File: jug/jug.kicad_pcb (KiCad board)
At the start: 2 copper layers, 154.4 x 108.2 mm, 96 parts, among them J1 USB_A, J2 USB_A, U1 RP2040_Pro_Micro, U2 RP2040_Pro_Micro

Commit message: finished pcb with RP2040 Pro Micro
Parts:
- removed D28, D29, D30, D31, D32, D33, D34, D35, D36, D37, D38, D39, D40, D41, D42, D43, D44, D45, D46, D47: D, ScottoKeebs_Components:Double_Sided_Diode_DO-35
- removed J2: USB_A, Connector_USB:USB_A_Molex_67643_Horizontal
- removed S24, S25, S26, S27, S28, S29, S30, S31, S32, S33, S34, S35, S36, S37, S38, S39, S40, S41, S42, S43, S44: Keyswitch, ScottoKeebs_Hotswap:Hotswap_MX_Plated_1.00u
- removed S45, S46: Keyswitch, ScottoKeebs_Hotswap:Hotswap_MX_Plated_1.50u_90deg
- removed U1: RP2040_Pro_Micro, ScottoKeebs_MCU:RP2040_Pro_Micro
- added D26: LED, LED_SMD:LED_1206_3216Metric_Pad1.42x1.75mm_HandSolder, F.Cu at (181.7, 114.8)
- added G***: LOGO, LOGO, F.Cu at (190.1, 74.7)
- added G***: LOGO, LOGO, B.Cu at (190.1, 74.7)
- added JP1: SolderJumper_2_Open, Jumper:SolderJumper-2_P1.3mm_Open_TrianglePad1.0x1.5mm, F.Cu at (181.0, 105.1)
- added JP2: SolderJumper_2_Open, Jumper:SolderJumper-2_P1.3mm_Open_TrianglePad1.0x1.5mm, F.Cu at (184.8, 105.1)
- added JP3: SolderJumper_2_Open, Jumper:SolderJumper-2_P1.3mm_Open_TrianglePad1.0x1.5mm, B.Cu at (181.0, 105.1)
- added JP4: SolderJumper_2_Open, Jumper:SolderJumper-2_P1.3mm_Open_TrianglePad1.0x1.5mm, B.Cu at (184.8, 105.1)
- added JP5: SolderJumper_2_Open, Jumper:SolderJumper-2_P1.3mm_Open_TrianglePad1.0x1.5mm, F.Cu at (181.0, 108.5)
- added JP6: SolderJumper_2_Open, Jumper:SolderJumper-2_P1.3mm_Open_TrianglePad1.0x1.5mm, F.Cu at (184.8, 108.5)
- added JP7: SolderJumper_2_Open, Jumper:SolderJumper-2_P1.3mm_Open_TrianglePad1.0x1.5mm, B.Cu at (181.0, 108.5)
- added JP8: SolderJumper_2_Open, Jumper:SolderJumper-2_P1.3mm_Open_TrianglePad1.0x1.5mm, B.Cu at (184.8, 108.5)
- added R1: R, Resistor_SMD:R_1206_3216Metric_Pad1.30x1.75mm_HandSolder, B.Cu at (186.4, 123.2)
- added R2: R, Resistor_SMD:R_1206_3216Metric_Pad1.30x1.75mm_HandSolder, B.Cu at (188.9, 120.7)
- added R3: R, Resistor_SMD:R_1206_3216Metric_Pad1.30x1.75mm_HandSolder, F.Cu at (186.4, 123.2)
- added R4: R, Resistor_SMD:R_1206_3216Metric_Pad1.30x1.75mm_HandSolder, F.Cu at (188.9, 120.7)
- D24, D25: value D -> LED; footprint ScottoKeebs_Components:Double_Sided_Diode_DO-35 -> LED_SMD:LED_1206_3216Metric_Pad1.42x1.75mm_HandSolder; moved to B.Cu
- D27: value D -> LED; footprint ScottoKeebs_Components:Double_Sided_Diode_DO-35 -> LED_SMD:LED_1206_3216Metric_Pad1.42x1.75mm_HandSolder
- S10, S11, S12, S13, S14, S15, S16, S17, S18, S19, S2, S20, S21, S3, S4, S5, S6, S7, S8, S9: footprint ScottoKeebs_Hotswap:Hotswap_MX_Plated_1.00u -> ScottoKeebs_Hotswap:Hotswap_MX_Plated_1.00u_Reversible
- S22, S23: footprint ScottoKeebs_Hotswap:Hotswap_MX_Plated_1.50u_90deg -> ScottoKeebs_Hotswap:Hotswap_MX_Plated_1.50u_90deg_Reversible
- U2: value RP2040_Pro_Micro -> Arduino_Pro_Micro; footprint ScottoKeebs_MCU:RP2040_Pro_Micro -> keyboard_reversible:ProMicro_flipped
- moved U2 318.6 mm to (190.2, 85.7), turned to -90 degrees
- moved D25 310.3 mm to (185.5, 114.8), turned to 90 degrees
- moved D27 309.1 mm to (185.5, 114.8), turned to 90 degrees
- moved D24 292.0 mm to (181.7, 114.8), turned to 90 degrees
- moved J1 45.2 mm to (189.8, 113.8)
- moved S22 42.8 mm to (183.8, 135.7), turned to -26.5 degrees
- moved S14 42.8 mm to (92.7, 115.7), turned to 0 degrees
- moved S4 42.8 mm to (130.8, 65.7), turned to 0 degrees
- moved D2 42.8 mm to (102.2, 81.4)
- moved S16 42.8 mm to (130.8, 103.8), turned to 0 degrees
- moved S8 42.8 mm to (92.7, 96.6), turned to 0 degrees
- moved D1 42.8 mm to (83.2, 83.8)
- moved D6 42.8 mm to (178.4, 81.4)
- moved D12 42.8 mm to (178.4, 100.4)
- moved S5 42.8 mm to (149.9, 72.8), turned to 0 degrees
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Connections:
- D24 pad 1: ROW0R -> Net-(D24-K)
- D24 pad 2: Net-(D24-A) -> LED0
- D25 pad 1: ROW1R -> Net-(D25-K)
- D25 pad 2: Net-(D25-A) -> LED1
- D27 pad 1: ROW2R -> Net-(D27-K)
- D27 pad 2: Net-(D27-A) -> LED1
- J1 pad 1: +5V -> Net-(J1-VBUS)
- J1 pad 2: INTERCONNECT_A -> Net-(J1-D-)
- J1 pad 3: INTERCONNECT_B -> Net-(J1-D+)
- J1 pad 4: GND -> Net-(J1-GND)
- U2 pad 10: COL2R -> unconnected-(U2-7/PE6-Pad10)_1
- U2 pad 11: COL3R -> LED0
- U2 pad 12: COL4R -> LED1
- U2 pad 13: COL5R -> COL5L
- U2 pad 14: unconnected-(U2-GP12-Pad14) -> COL4L
- U2 pad 15: unconnected-(U2-GP13-Pad15) -> COL3L
- U2 pad 16: unconnected-(U2-GP14-Pad16) -> COL2L
- U2 pad 17: unconnected-(U2-GP15-Pad17) -> COL1L
- U2 pad 18: unconnected-(U2-GP16-Pad18) -> COL0L
- U2 pad 19: unconnected-(U2-GP21-Pad19) -> INTERCONNECT_B
- U2 pad 20: unconnected-(U2-GP23-Pad20) -> INTERCONNECT_A
- U2 pad 22: ROW3R -> unconnected-(U2-RST-Pad22)_1
- U2 pad 23: ROW2R -> GND
- U2 pad 24: ROW1R -> +5V
- U2 pad 3: unconnected-(U2-GP1-Pad3) -> GND
- U2 pad 5: GND -> unconnected-(U2-2/PD1-Pad5)_1
- U2 pad 6: INTERCONNECT_A2 -> ROW0L
- U2 pad 7: INTERCONNECT_B2 -> ROW1L
- U2 pad 8: COL0R -> ROW2L
- U2 pad 9: COL1R -> ROW3L
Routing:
- net COL4L: track 185.7 -> 128.6 mm
- net GND: track 0.00 -> 49.2 mm, vias 0 -> 4
- net COL2L: track 227.8 -> 184.5 mm
- net LED0: track 0.00 -> 33.0 mm, vias 0 -> 1
- net COL1L: track 234.7 -> 203.5 mm
- net COL0L: track 244.7 -> 217.5 mm
- net LED1: track 0.00 -> 19.6 mm, vias 0 -> 1
- net COL5L: track 75.0 -> 60.1 mm
- net Net-(J1-D-): track 0.00 -> 13.2 mm, vias 0 -> 1
- net Net-(J1-D+): track 0.00 -> 12.6 mm, vias 0 -> 1
- net Net-(J1-VBUS): track 0.00 -> 11.2 mm, vias 0 -> 1
- net Net-(J1-GND): track 0.00 -> 10.4 mm, vias 0 -> 1
- net Net-(D17-A): track 15.7 -> 6.24 mm
- net Net-(D19-A): track 15.7 -> 6.24 mm
- net Net-(D21-A): track 15.7 -> 6.24 mm
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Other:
- board size 154.4 x 108.2 mm -> 153.5 x 107.4 mm
- board text added: "Bridge jumpers on side with mcu"

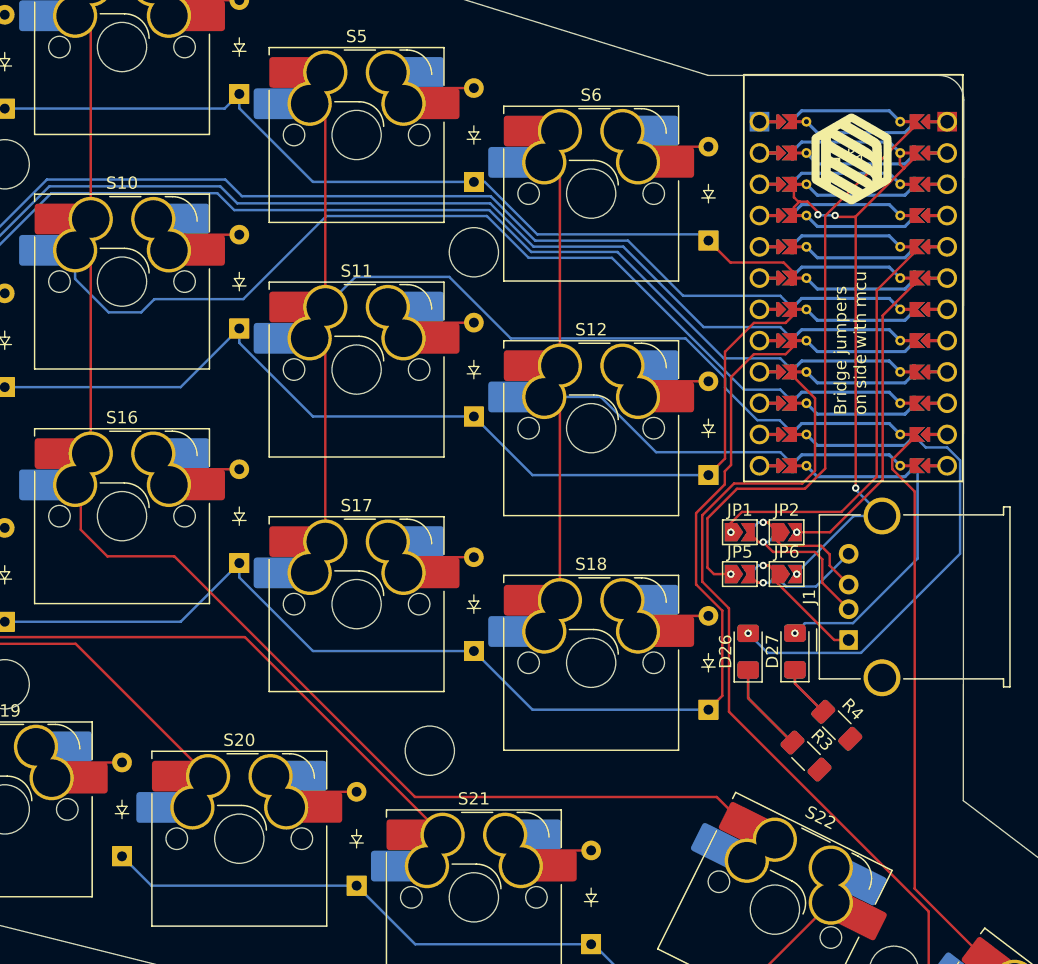
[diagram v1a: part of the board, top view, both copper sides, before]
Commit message: changed mcu to rp2040 zero with reversible footprint
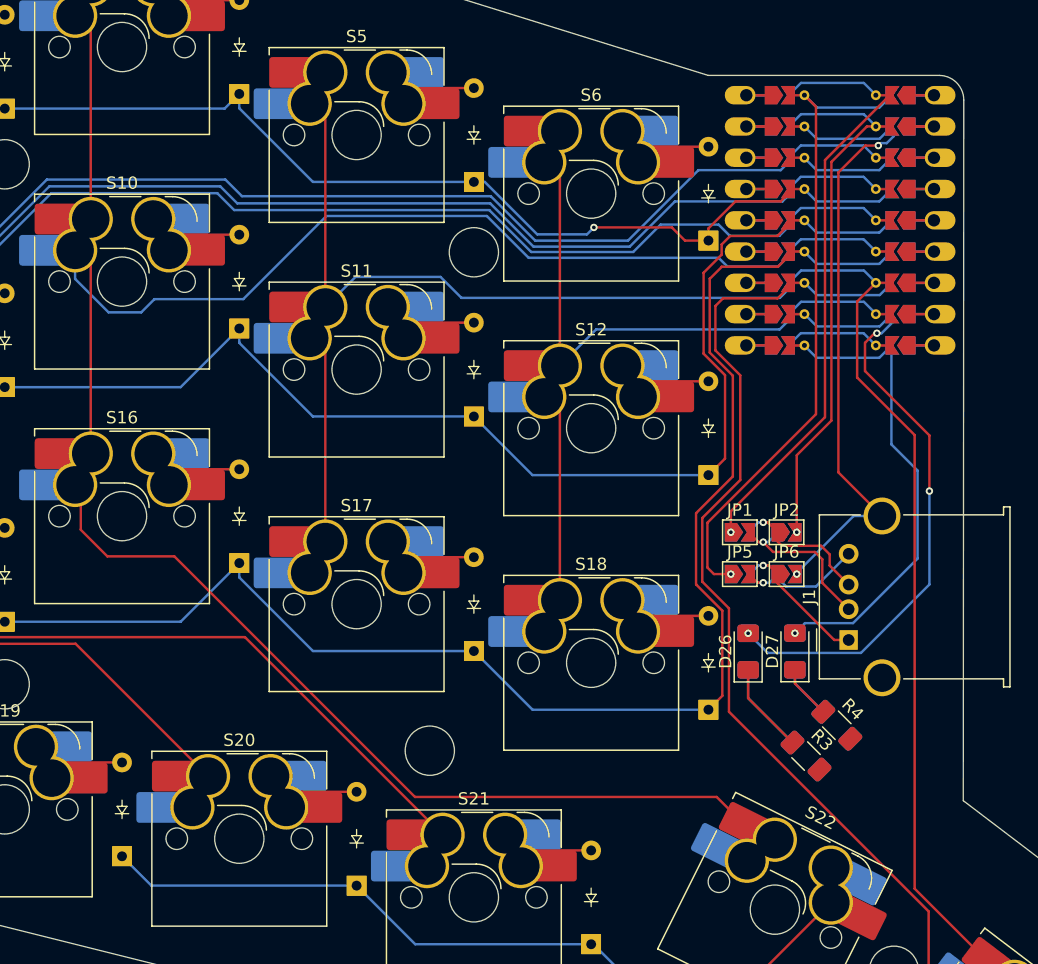
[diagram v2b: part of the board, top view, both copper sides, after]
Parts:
- removed G*** (x2): LOGO, LOGO
- removed U2: Arduino_Pro_Micro, keyboard_reversible:ProMicro_flipped
- added U1: RP2040_Zero, ScottoKeebs_MCU:RP2040_Zero_Reversible, F.Cu at (189.1, 79.7)
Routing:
- net LED1: track 19.6 -> 30.4 mm
- net ROW2L: track 142.5 -> 152.3 mm
- net LED0: track 33.0 -> 42.8 mm, vias 1 -> 3
- net INTERCONNECT_B: track 25.8 -> 35.7 mm
- net ROW1L: track 124.2 -> 133.5 mm
- net COL4L: track 128.6 -> 137.9 mm
- net INTERCONNECT_A: track 33.7 -> 40.8 mm
- net ROW3L: track 148.5 -> 155.3 mm
- net GND: track 49.2 -> 44.6 mm, vias 4 -> 2
- net COL3L: track 178.0 -> 173.9 mm
- net +5V: track 48.0 -> 44.2 mm
- net COL2L: track 184.5 -> 182.6 mm
- net ROW0L: track 114.8 -> 116.7 mm, vias 0 -> 1
- net COL5L: track 60.1 -> 58.6 mm
- net COL1L: track 203.5 -> 202.6 mm
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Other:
- board text removed: "Bridge jumpers on side with mcu"

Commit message: finished pcb
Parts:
- added G***: LOGO, LOGO, F.Cu at (189.1, 74.0)
- added G***: LOGO, LOGO, B.Cu at (189.1, 74.0)
- D25, R2: moved to F.Cu
- D26, R3: moved to B.Cu
- moved D26 20.8 mm to (191.1, 96.2)
- moved D27 19.3 mm to (191.1, 96.2)
- moved D24 19.0 mm to (185.9, 96.2)
- moved D25 18.5 mm to (185.9, 96.2)
- moved R3 8.19 mm to (182.1, 116.2), turned to -90 degrees
- moved R4 8.11 mm to (182.1, 116.2), turned to -90 degrees
- moved R1 7.02 mm to (185.9, 116.2), turned to -90 degrees
- moved R2 5.41 mm to (185.9, 116.2), turned to -90 degrees
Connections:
- D25 pad 2: LED1 -> LED0
- D26 pad 2: LED0 -> LED1
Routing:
- net LED0: track 42.8 -> 8.01 mm, vias 3 -> 2
- net Net-(D27-K): track 4.37 -> 29.6 mm
- net LED1: track 30.4 -> 5.77 mm
- net Net-(D26-K): track 7.39 -> 30.9 mm
- net Net-(D24-K): track 7.39 -> 30.6 mm
- net Net-(D25-K): track 4.37 -> 25.4 mm
- net INTERCONNECT_B: track 35.7 -> 39.8 mm
- net GND: track 44.6 -> 42.5 mm
- net INTERCONNECT_A: track 40.8 -> 42.5 mm
- net +5V: track 44.2 -> 45.8 mm
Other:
- board text added: ":D"
- board text added: "Bridge jumpers on side with MCU"
- board text added: "USB on top of PCB"

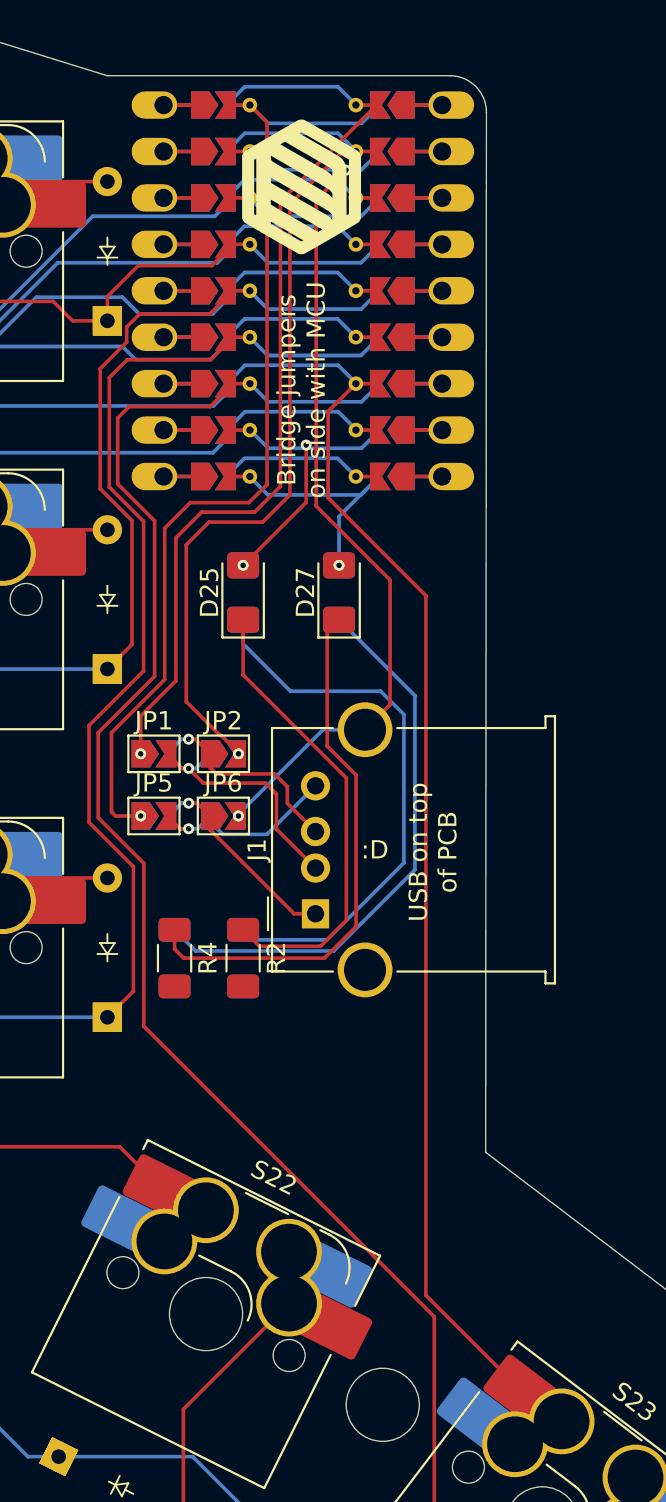
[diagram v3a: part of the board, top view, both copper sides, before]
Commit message: changed usb a to c
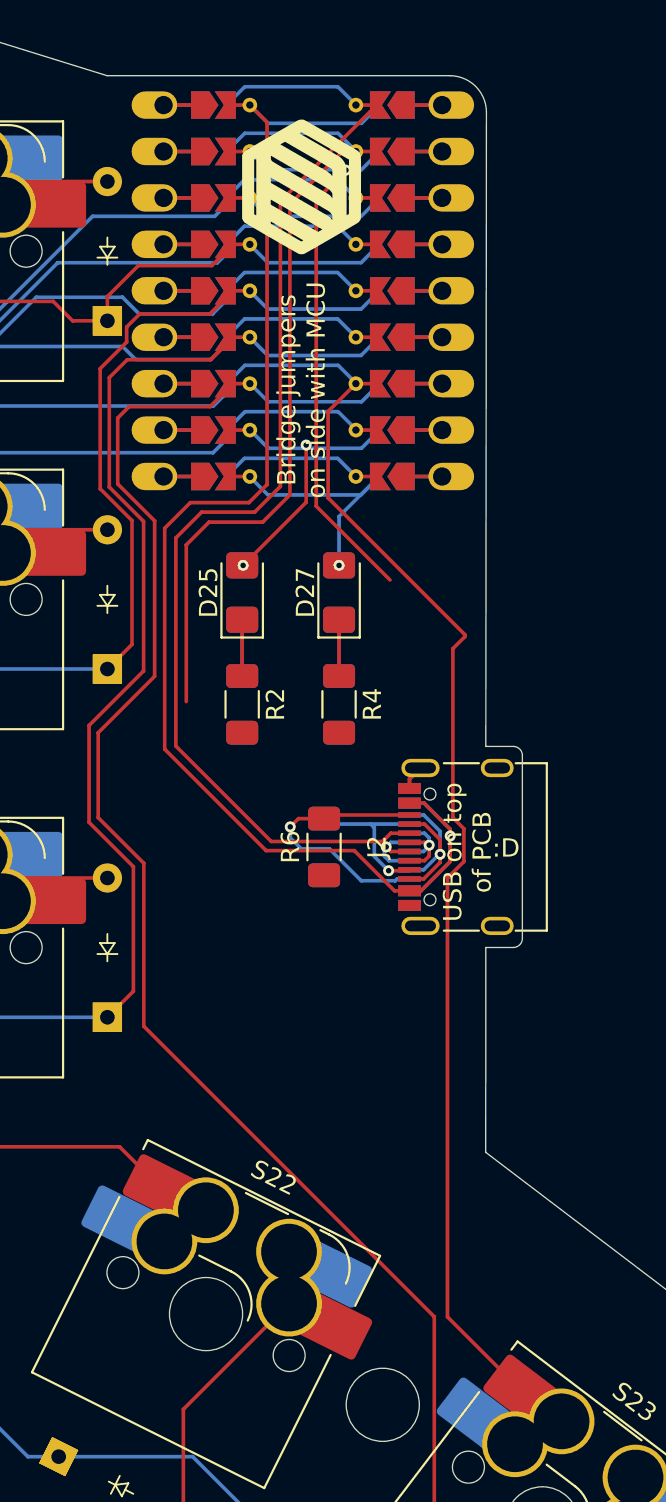
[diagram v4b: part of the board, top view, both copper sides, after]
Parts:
- removed J1: USB_A, Connector_USB:USB_A_Molex_67643_Horizontal
- removed JP1, JP2, JP3, JP4, JP5, JP6, JP7, JP8: SolderJumper_2_Open, Jumper:SolderJumper-2_P1.3mm_Open_TrianglePad1.0x1.5mm
- added J2: USB_C_Receptacle_USB2.0_14P, ScottoKeebs_Components:USB_C_Receptacle_G-Switch_GT-USB-7010ASV_Double-Sided, F.Cu at (198.7, 110.2)
- added R5: R, Resistor_SMD:R_1206_3216Metric_Pad1.30x1.75mm_HandSolder, B.Cu at (190.3, 110.2)
- added R6: R, Resistor_SMD:R_1206_3216Metric_Pad1.30x1.75mm_HandSolder, F.Cu at (190.3, 110.2)
- moved R3 16.5 mm to (191.1, 102.4)
- moved R4 16.5 mm to (191.1, 102.4)
- moved R1 13.9 mm to (185.8, 102.4)
- moved R2 13.9 mm to (185.8, 102.4)
- moved D24 0.05 mm to (185.8, 96.2)
- moved D25 0.05 mm to (185.8, 96.2)
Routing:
- net Net-(D26-K): track 30.9 -> 3.08 mm
- net Net-(D24-K): track 30.6 -> 3.08 mm
- net Net-(D27-K): track 29.6 -> 3.08 mm
- net +5V: track 45.8 -> 71.0 mm
- net Net-(D25-K): track 25.4 -> 3.08 mm
- net INTERCONNECT_A: track 42.5 -> 61.7 mm
- net GND: track 42.5 -> 27.5 mm, vias 2 -> 1
- net Net-(J2-CC2): track 0.00 -> 14.9 mm, vias 0 -> 1
- net Net-(J1-D-): track 13.2 -> 0.00 mm, vias 1 -> 0
- net Net-(J1-D+): track 12.6 -> 0.00 mm, vias 1 -> 0
- net Net-(J1-VBUS): track 11.2 -> 0.00 mm, vias 1 -> 0
- net (no net): track 0.00 -> 10.6 mm, vias 0 -> 1
- net Net-(J1-GND): track 10.4 -> 0.00 mm, vias 1 -> 0
- net Net-(J2-CC1): track 0.00 -> 8.92 mm, vias 0 -> 1
- net Net-(J2-D--PadA7): track 0.00 -> 5.68 mm, vias 0 -> 1
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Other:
- outline, holes or cut-outs redrawn
